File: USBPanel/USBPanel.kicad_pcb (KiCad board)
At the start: 6 copper layers, 36 x 38 mm, 70 parts, among them J1 PORT1, J2 PORT2, J3 PWR, J4 USB_UFP, J5 SINK, J6 I2Ct, J7 I2Cc, Q1 ISZ0702NLS, Q2 ISZ0702NLS, Q3 NX138BK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

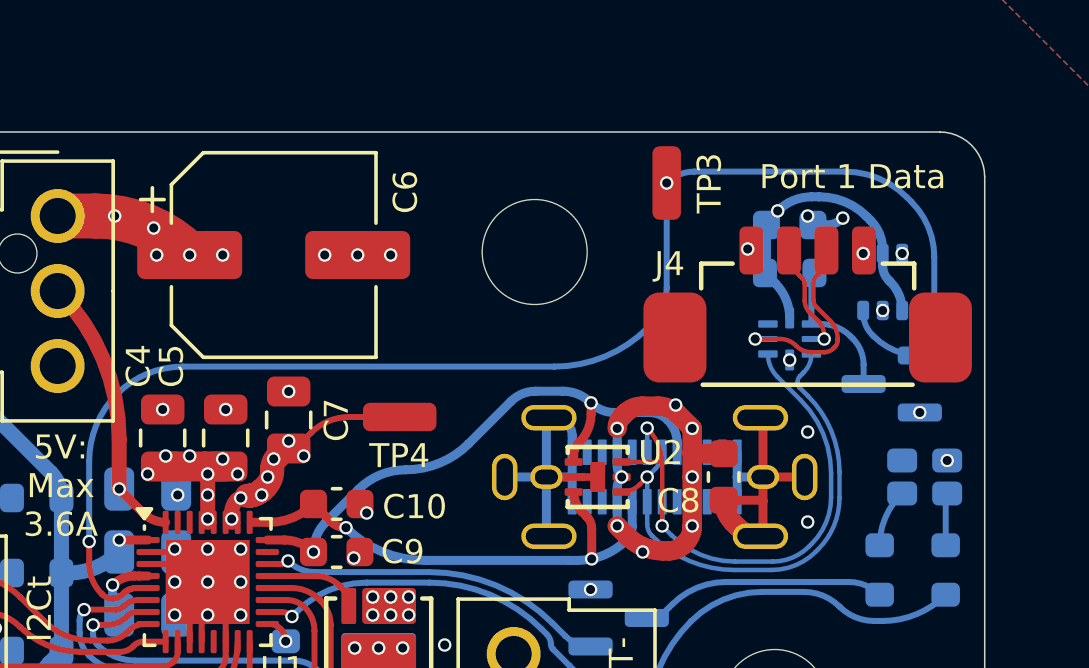
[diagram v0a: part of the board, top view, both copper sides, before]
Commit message: USBPanel configuration and post-build edits
Changed LED colour assignments and resistor values.
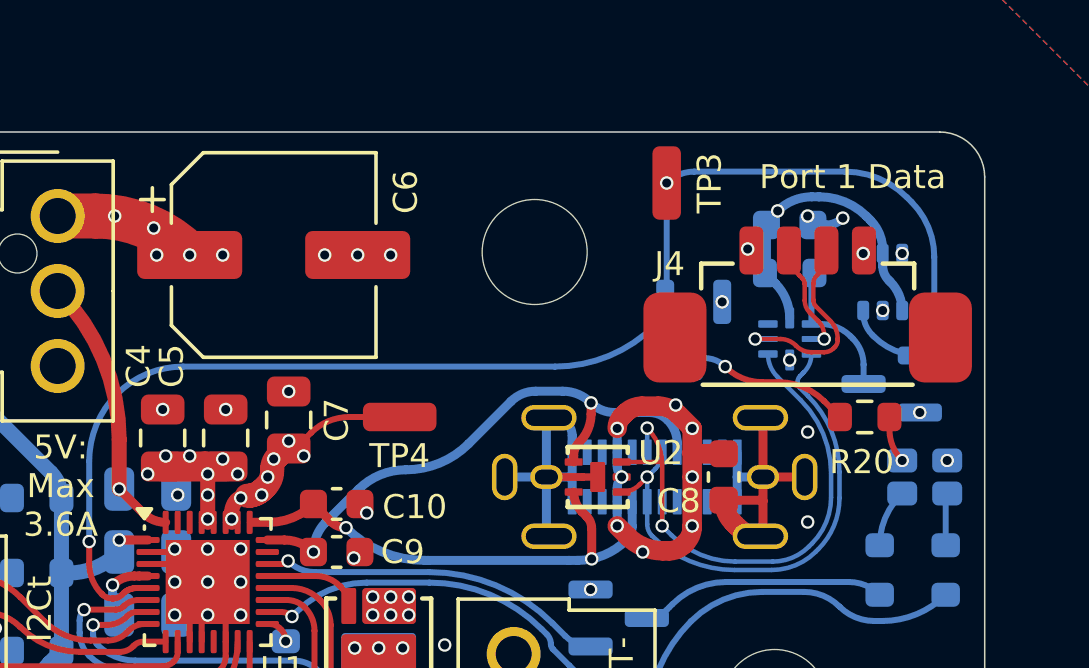
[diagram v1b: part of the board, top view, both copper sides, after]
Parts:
- added Q6: NX138BK, Package_TO_SOT_SMD:SOT-23, B.Cu at (156.3, 87.6)
- added R20: 2.2kΩ, Resistor_SMD:R_0603_1608Metric, F.Cu at (162.0, 90.5)
- R13, R14, R15, R16: value 470Ω -> 4.7kΩ
- R17: value 220Ω? -> 2.2kΩ
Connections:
- D2 pad 2: unconnected-(D2-BK-Pad2) -> Net-(D2-BK)
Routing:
- net Net-(Q6-D): track 0.00 -> 5.46 mm, vias 0 -> 1
- net Net-(D2-BK): track 0.00 -> 1.56 mm, vias 0 -> 1
- net GND: vias 55 -> 56
